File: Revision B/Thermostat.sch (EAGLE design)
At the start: 27 parts, among them K1 G5LE, K2 G5LE, K3 G5LE, P4 M01PTH, P5 M01PTH, P6 M01PTH, P7 M01PTH, T1 MOSFET, T2 MOSFET, T3 MOSFET

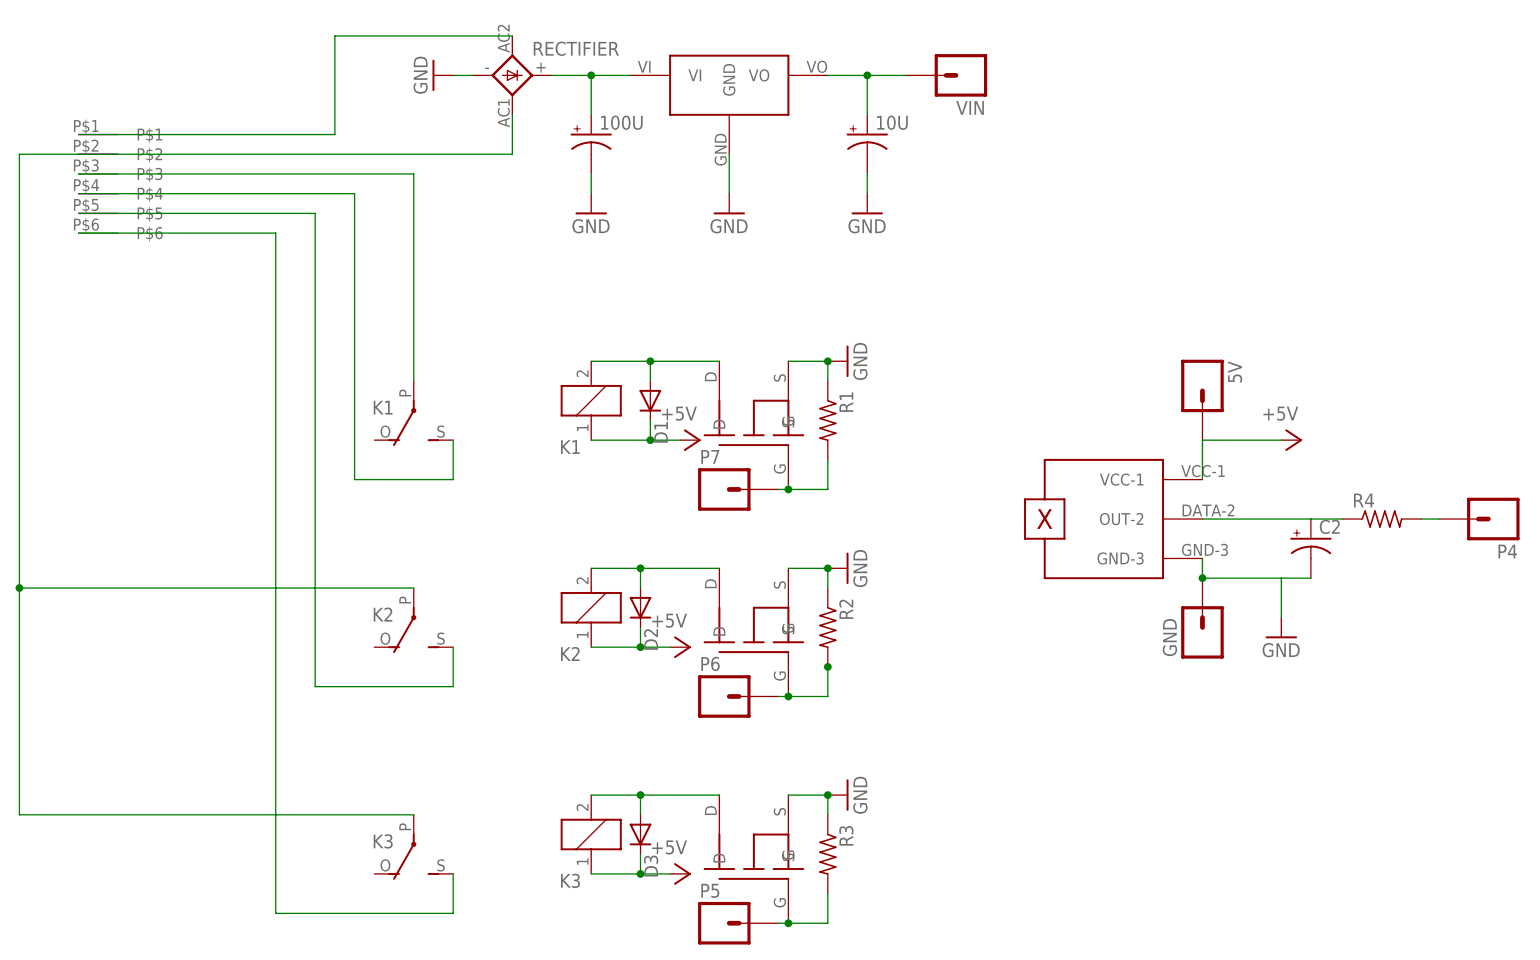
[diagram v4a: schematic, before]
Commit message: Made tweeks after first print
Moved relay bodies off the board to provide more space.
Widened holes for temp sensor, transistors, capacitor and terminal
Spread out components that were overlapping.
Removed wires crossing low-pass filter.
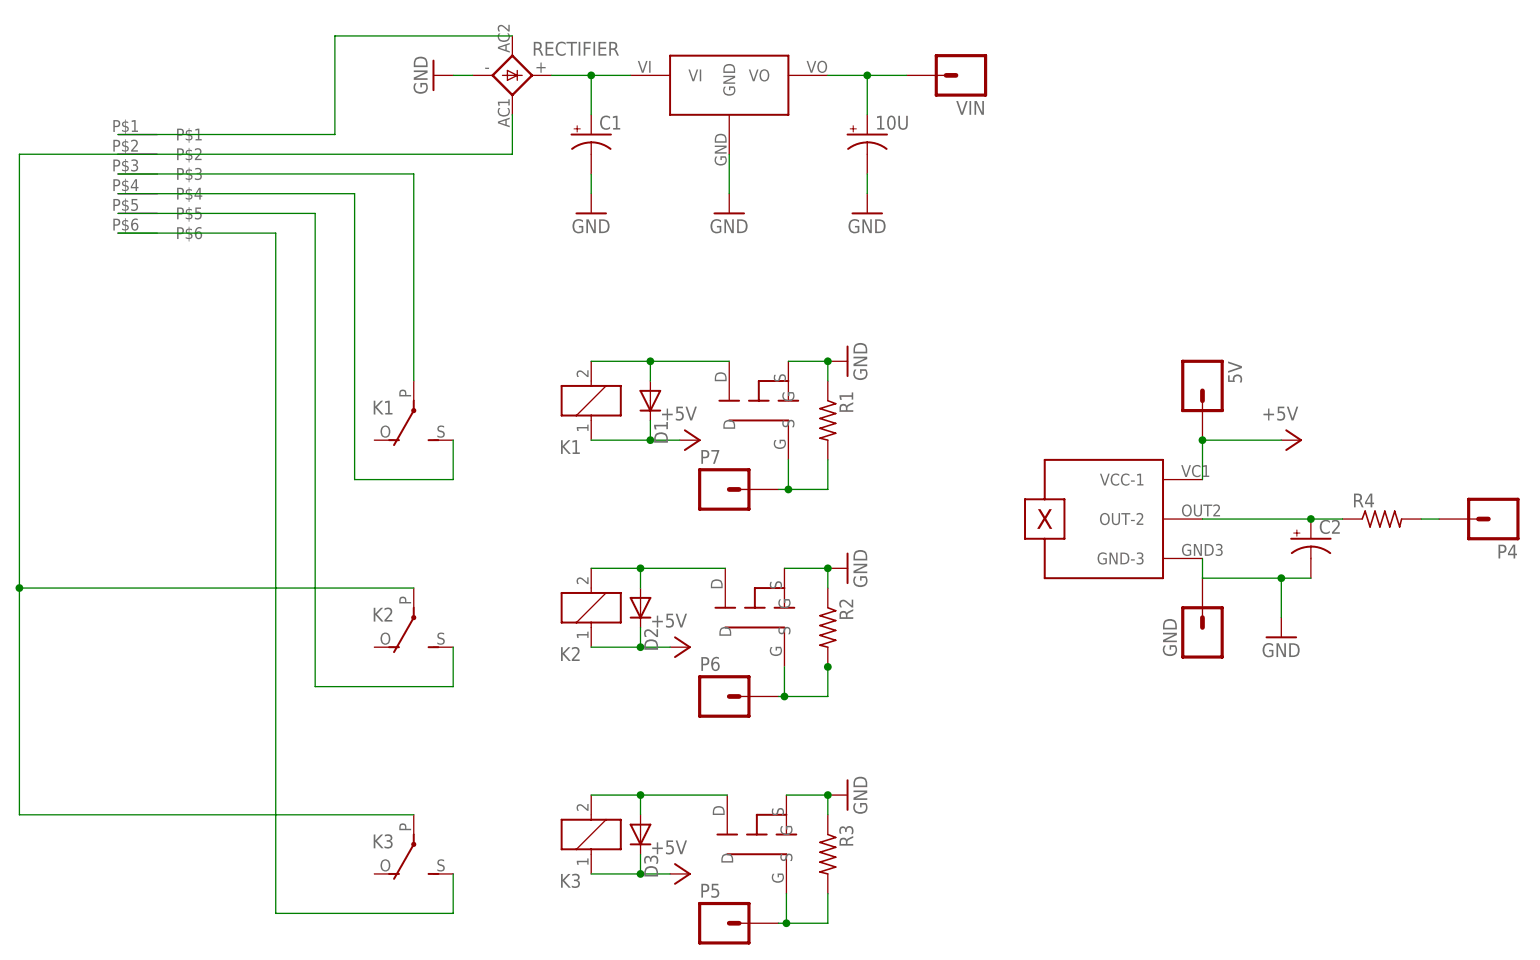
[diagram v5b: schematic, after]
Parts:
- removed 100U: (no value), SparkFun-Passives:CAP_POLPTH1
- removed T1, T2, T3: MOSFET, android-thermostat:MOSFET
- added C1: (no value), rcl:CPOL-USE5-10.5
- added U$4, U$5, U$6: TRANSISTOR, android-thermostat:TRANSISTOR
- R4: device rcl:R-US_0204/5 -> rcl:R-US_0204/7
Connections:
- removed net N$16: 5V.1, U$1.VCC-1
- net +5V: now also 5V.1, U$1.VCC-1
- net GND: now also C1.-, U$4.S, U$5.S, U$6.S; no longer 100U.-, T1.S, T2.S, T3.S
- net N$17: now also U$4.G; no longer T3.G
- net N$18: now also U$4.D; no longer T3.D
- net N$2: now also U$5.G; no longer T2.G
- net N$24: now also C1.+; no longer 100U.+
- net N$3: now also U$5.D; no longer T2.D
- net N$6: now also U$6.G; no longer T1.G
- net N$7: now also U$6.D; no longer T1.D

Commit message: Moved Temperature Pin
Moved the temperature sensor input from PIN 4 (digital) to PIN 43
(analog).  This required moving a number of components around on the
board.
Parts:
- renumbered P4 to P43
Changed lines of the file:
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@@
 <part name="5V" library="SparkFun-Connectors" deviceset="M01" device="PTH" value=""/>
 <part name="GND" library="SparkFun-Connectors" deviceset="M01" device="PTH" value=""/>
-<part name="P4" library="SparkFun-Connectors" deviceset="M01" device="PTH" value=""/>
+<part name="P43" library="SparkFun-Connectors" deviceset="M01" device="PTH" value=""/>
 <part name="P6" library="SparkFun-Connectors" deviceset="M01" device="PTH" value=""/>
 <part name="P5" library="SparkFun-Connectors" deviceset="M01" device="PTH" value=""/>
@@
 <instance part="5V" gate="G$1" x="111.76" y="54.61" rot="R270"/>
 <instance part="GND" gate="G$1" x="111.76" y="21.59" rot="R90"/>
-<instance part="P4" gate="G$1" x="149.86" y="36.83" rot="R180"/>
+<instance part="P43" gate="G$1" x="149.86" y="36.83" rot="R180"/>
 <instance part="P6" gate="G$1" x="49.53" y="13.97"/>
 <instance part="P5" gate="G$1" x="49.53" y="-15.24"/>
@@
 <net name="N$5" class="0">
 <segment>
-<pinref part="P4" gate="G$1" pin="1"/>
+<pinref part="P43" gate="G$1" pin="1"/>
 <wire x1="139.954" y1="36.83" x2="142.24" y2="36.83" width="0.3048" layer="91"/>
 <pinref part="R4" gate="G$1" pin="2"/>

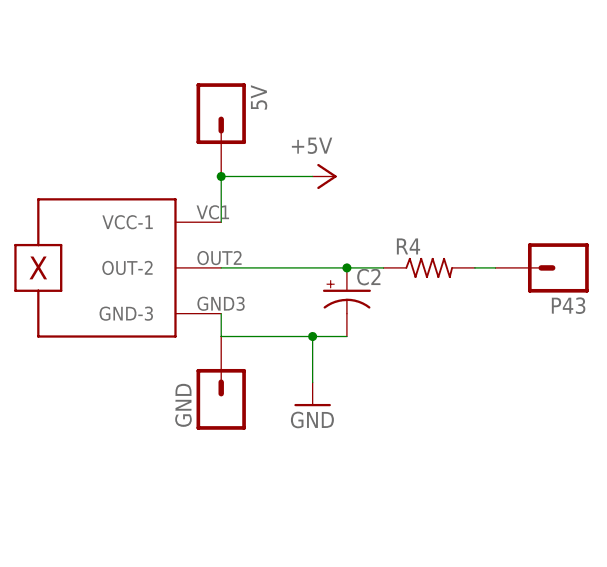
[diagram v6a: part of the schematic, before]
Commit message: Low-pass filter changes
Made adjustments to the low-pass filter per suggestions at:
http://www.reddit.com/r/AndroidThermostat/comments/19ntz4/temp_sensor_filter/
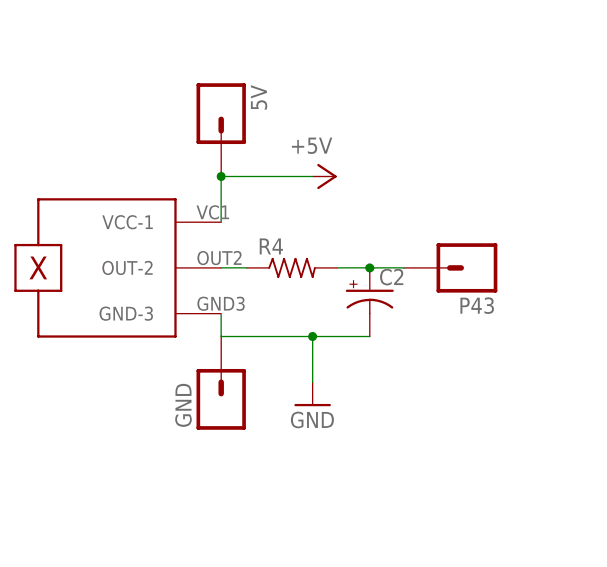
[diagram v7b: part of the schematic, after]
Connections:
- net N$4: now also P43.1, R4.2; no longer R4.1, U$1.OUT-2
- net N$5: now also R4.1, U$1.OUT-2; no longer P43.1, R4.2
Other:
- moved on the sheet: C2, P43, R4
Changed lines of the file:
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@@
 <setting verticaltext="up"/>
 </settings>
-<grid distance="0.1" unitdist="inch" unit="inch" style="lines" multiple="1" display="no" altdistance="0.01" altunitdist="inch" altunit="inch"/>
+<grid distance="0.01" unitdist="inch" unit="inch" style="lines" multiple="1" display="yes" altdistance="0.01" altunitdist="inch" altunit="inch"/>
 <layers>
 <layer number="1" name="Top" color="4" fill="1" visible="no" active="no"/>
@@
 <instance part="5V" gate="G$1" x="111.76" y="54.61" rot="R270"/>
 <instance part="GND" gate="G$1" x="111.76" y="21.59" rot="R90"/>
-<instance part="P43" gate="G$1" x="149.86" y="36.83" rot="R180"/>
+<instance part="P43" gate="G$1" x="139.7" y="36.83" rot="R180"/>
 <instance part="P6" gate="G$1" x="49.53" y="13.97"/>
 <instance part="P5" gate="G$1" x="49.53" y="-15.24"/>
@@
 <instance part="R2" gate="G$1" x="63.5" y="22.86" rot="R270"/>
 <instance part="R3" gate="G$1" x="63.5" y="-6.35" rot="R270"/>
-<instance part="C2" gate="G$1" x="125.73" y="34.29"/>
+<instance part="C2" gate="G$1" x="128.27" y="34.29"/>
 <instance part="U$3" gate="G$1" x="-27.94" y="81.28"/>
 <instance part="U$1" gate="G$1" x="99.06" y="36.83"/>
@@
 <instance part="U$5" gate="G$1" x="54.102" y="25.4" rot="R90"/>
 <instance part="U$6" gate="G$1" x="54.61" y="52.07" rot="R90"/>
-<instance part="R4" gate="G$1" x="134.874" y="36.83"/>
+<instance part="R4" gate="G$1" x="119.634" y="36.83"/>
 <instance part="C1" gate="G$1" x="33.02" y="86.36"/>
 </instances>
@@
 <wire x1="121.92" y1="29.21" x2="121.92" y2="24.13" width="0.3048" layer="91"/>
 <pinref part="C2" gate="G$1" pin="-"/>
-<wire x1="121.92" y1="29.21" x2="125.73" y2="29.21" width="0.3048" layer="91"/>
+<wire x1="121.92" y1="29.21" x2="128.27" y2="29.21" width="0.3048" layer="91"/>
 <pinref part="U$1" gate="G$1" pin="GND-3"/>
 <wire x1="111.76" y1="31.75" x2="111.76" y2="29.21" width="0.3048" layer="91"/>
@@
 <junction x="33.02" y="93.98"/>
 <pinref part="C1" gate="G$1" pin="+"/>
-</segment>
-</net>
-<net name="N$4" class="0">
-<segment>
-<pinref part="C2" gate="G$1" pin="+"/>
-<wire x1="129.794" y1="36.83" x2="125.73" y2="36.83" width="0.3048" layer="91"/>
-<pinref part="U$1" gate="G$1" pin="OUT-2"/>
-<wire x1="111.76" y1="36.83" x2="125.73" y2="36.83" width="0.3048" layer="91"/>
-<junction x="125.73" y="36.83"/>
-<pinref part="R4" gate="G$1" pin="1"/>
-</segment>
-</net>
-<net name="N$5" class="0">
-<segment>
-<pinref part="P43" gate="G$1" pin="1"/>
-<wire x1="139.954" y1="36.83" x2="142.24" y2="36.83" width="0.3048" layer="91"/>
-<pinref part="R4" gate="G$1" pin="2"/>
 </segment>
 </net>
@@
 </segment>
 </net>
+<net name="N$4" class="0">
+<segment>
+<pinref part="R4" gate="G$1" pin="2"/>
+<pinref part="C2" gate="G$1" pin="+"/>
+<wire x1="124.714" y1="36.83" x2="128.27" y2="36.83" width="0.1524" layer="91"/>
+<pinref part="P43" gate="G$1" pin="1"/>
+<wire x1="128.27" y1="36.83" x2="132.08" y2="36.83" width="0.1524" layer="91"/>
+<junction x="128.27" y="36.83"/>
+</segment>
+</net>
+<net name="N$5" class="0">
+<segment>
+<pinref part="U$1" gate="G$1" pin="OUT-2"/>
+<pinref part="R4" gate="G$1" pin="1"/>
+<wire x1="111.76" y1="36.83" x2="114.554" y2="36.83" width="0.1524" layer="91"/>
+</segment>
+</net>

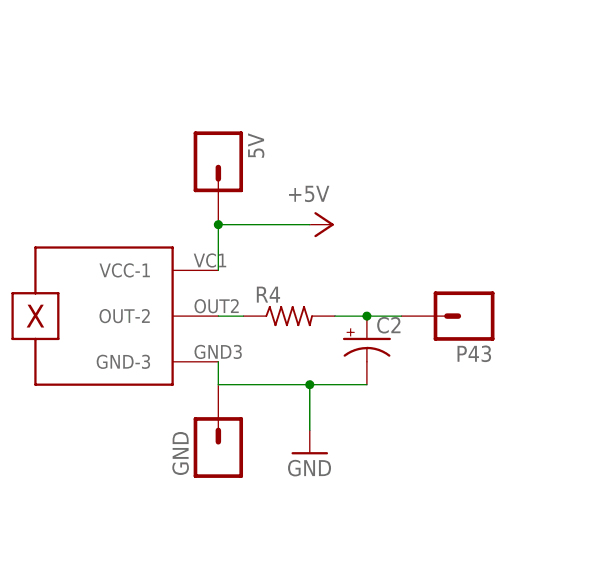
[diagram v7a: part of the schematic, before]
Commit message: Added Capacitor
Added a 0.1uF capacitor between the 5v and GND lines on the temperature
sensor to help avoid fluctuations.
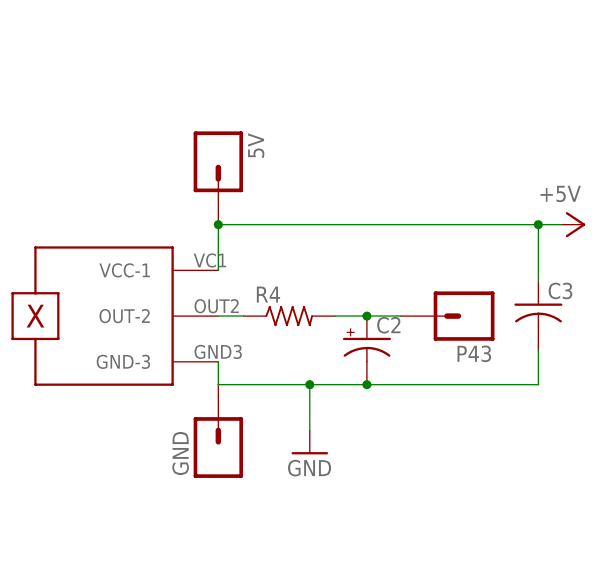
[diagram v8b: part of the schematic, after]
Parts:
- added C3: (no value), rcl:C-US050-024X044
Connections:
- net +5V: now also C3.1
- net GND: now also C3.2
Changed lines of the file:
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@@
 <setting verticaltext="up"/>
 </settings>
-<grid distance="0.01" unitdist="inch" unit="inch" style="lines" multiple="1" display="yes" altdistance="0.01" altunitdist="inch" altunit="inch"/>
+<grid distance="0.1" unitdist="inch" unit="inch" style="lines" multiple="1" display="no" altdistance="0.01" altunitdist="inch" altunit="inch"/>
 <layers>
 <layer number="1" name="Top" color="4" fill="1" visible="no" active="no"/>
@@
 <part name="R4" library="rcl" deviceset="R-US_" device="0204/7"/>
 <part name="C1" library="rcl" deviceset="CPOL-US" device="E5-10.5"/>
+<part name="C3" library="rcl" deviceset="C-US" device="050-024X044"/>
 </parts>
 <sheets>
@@
 <instance part="P+2" gate="1" x="45.72" y="20.32" rot="R270"/>
 <instance part="P+3" gate="1" x="45.72" y="-8.89" rot="R270"/>
-<instance part="P+4" gate="1" x="124.46" y="46.99" rot="R270"/>
+<instance part="P+4" gate="1" x="152.4" y="46.99" rot="R270"/>
 <instance part="R1" gate="G$1" x="63.5" y="49.53" rot="R270"/>
 <instance part="R2" gate="G$1" x="63.5" y="22.86" rot="R270"/>
@@
 <instance part="R4" gate="G$1" x="119.634" y="36.83"/>
 <instance part="C1" gate="G$1" x="33.02" y="86.36"/>
+<instance part="C3" gate="G$1" x="147.32" y="38.1"/>
 </instances>
 <busses>
@@
 <wire x1="111.76" y1="31.75" x2="111.76" y2="29.21" width="0.3048" layer="91"/>
 <junction x="121.92" y="29.21"/>
+<pinref part="C3" gate="G$1" pin="2"/>
+<wire x1="128.27" y1="29.21" x2="147.32" y2="29.21" width="0.3048" layer="91"/>
+<wire x1="147.32" y1="29.21" x2="147.32" y2="33.02" width="0.3048" layer="91"/>
+<junction x="128.27" y="29.21"/>
 </segment>
 <segment>
@@
 <wire x1="111.76" y1="41.91" x2="111.76" y2="46.99" width="0.3048" layer="91"/>
 <pinref part="P+4" gate="1" pin="+5V"/>
-<wire x1="121.92" y1="46.99" x2="111.76" y2="46.99" width="0.3048" layer="91"/>
+<wire x1="149.86" y1="46.99" x2="147.32" y2="46.99" width="0.3048" layer="91"/>
 <junction x="111.76" y="46.99"/>
-</segment>
-</net>
+<pinref part="C3" gate="G$1" pin="1"/>
+<wire x1="147.32" y1="46.99" x2="111.76" y2="46.99" width="0.3048" layer="91"/>
+<wire x1="147.32" y1="40.64" x2="147.32" y2="46.99" width="0.3048" layer="91"/>
+<junction x="147.32" y="46.99"/>
+</segment>
+</net>
